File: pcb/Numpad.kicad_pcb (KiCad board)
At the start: 2 copper layers, 57 parts, among them P1 USB-MICRO-B, SW1 F1, SW10 8, SW11 9, SW12 PLUS, SW13 4, SW14 5, SW15 6, SW16 ENTER, SW17 1, SW18 2, SW19 3, SW2 F2, SW20 0, SW21 PERIOD, SW22 SW_PUSH, SW3 F3, SW4 F4, SW5 NUMLOCK, SW6 SLASH, SW7 STAR, SW8 MINUS, SW9 7, U1 ATmega32U4-AU, X1 16MHz

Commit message: Lay out components mostly
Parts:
- C1, C2, C3, C4, C5, C6, D1, D10, D11, D12, D13, D14, D15, D16, D17, D18, D19, D2, D20, D21, D3, D4, D5, D6, D7, D8, D9, P1, R1, R2, R3, R4, SW22, U1, X1: moved to B.Cu
- moved SW22 161.9 mm to (103.5, 132.7), turned to 270 degrees
- moved U1 135.2 mm to (132.1, 134.0)
- moved D17 129.5 mm to (74.9, 149.9), turned to 180 degrees
- moved D13 128.1 mm to (74.9, 130.8), turned to 180 degrees
- moved X1 127.6 mm to (132.1, 102.9), turned to 180 degrees
- moved D9 126.9 mm to (74.9, 111.8), turned to 180 degrees
- moved D5 125.3 mm to (74.9, 92.7), turned to 180 degrees
- moved D1 123.8 mm to (74.9, 73.7), turned to 180 degrees
- moved D20 123.8 mm to (84.5, 168.9), turned to 180 degrees
- moved C1 116.0 mm to (118.7, 127.6), turned to 270 degrees
- moved D18 110.4 mm to (94.0, 149.9), turned to 180 degrees
- moved R4 109.6 mm to (103.5, 139.7)
- moved D14 109.0 mm to (94.0, 130.8), turned to 180 degrees
- moved D10 107.6 mm to (94.0, 111.8), turned to 180 degrees
- moved P1 107.4 mm to (103.5, 59.1), turned to 0 degrees
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
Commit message: Add SMD micro USB B, move MCU
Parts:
- P1: footprint Connect:USB_Micro-B -> 10118192-0001LF:10118192-0001LF
- moved SW22 29.9 mm to (98.9, 162.3)
- moved R4 29.6 mm to (98.9, 168.9)
- moved R1 5.08 mm to (85.7, 66.7)
- moved R2 5.08 mm to (83.2, 66.7)
- moved P1 2.41 mm to (103.5, 56.6)
- moved U1 1.15 mm to (132.0, 132.8), turned to 225 degrees

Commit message: Add OSH Park design rules
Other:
- net class Default: clearance 0.2 -> 0.1524; trace_width 0.25 -> 0.1524; via_dia 0.6 -> 0.6858; via_drill 0.4 -> 0.3302
- rule trace_clearance: 0.2 -> 0.1524
- rule trace_min: 0.2 -> 0.1524
- rule via_min_drill: 0.3 -> 0.3302
- rule via_min_size: 0.4 -> 0.6858
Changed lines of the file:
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@@
   )
   (setup
-    (last_trace_width 0.25)
-    (trace_clearance 0.2)
+    (last_trace_width 0.1524)
+    (trace_clearance 0.1524)
     (zone_clearance 0.508)
     (zone_45_only no)
-    (trace_min 0.2)
+    (trace_min 0.1524)
     (segment_width 0.2)
     (edge_width 0.1)
-    (via_size 0.6)
-    (via_drill 0.4)
-    (via_min_size 0.4)
-    (via_min_drill 0.3)
-    (uvia_size 0.3)
-    (uvia_drill 0.1)
+    (via_size 0.6858)
+    (via_drill 0.3302)
+    (via_min_size 0.6858)
+    (via_min_drill 0.3302)
+    (uvia_size 0.762)
+    (uvia_drill 0.508)
     (uvias_allowed no)
-    (uvia_min_size 0.2)
-    (uvia_min_drill 0.1)
+    (uvia_min_size 0)
+    (uvia_min_drill 0)
     (pcb_text_width 0.3)
     (pcb_text_size 1.5 1.5)
@@
   (net 61 "Net-(U1-Pad42)")
   (net_class Default "This is the default net class."
-    (clearance 0.2)
-    (trace_width 0.25)
-    (via_dia 0.6)
-    (via_drill 0.4)
-    (uvia_dia 0.3)
-    (uvia_drill 0.1)
+    (clearance 0.1524)
+    (trace_width 0.1524)
+    (via_dia 0.6858)
+    (via_drill 0.3302)
+    (uvia_dia 0.762)
+    (uvia_drill 0.508)
     (add_net +5V)
     (add_net /COL0)

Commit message: Routing
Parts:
- added P2: HOLE, Connect:1pin, F.Cu at (84.2, 75.7)
- added P3: HOLE, Connect:1pin, F.Cu at (122.3, 75.7)
- added P4: HOLE, Connect:1pin, F.Cu at (84.5, 145.8)
- added P5: HOLE, Connect:1pin, F.Cu at (121.8, 152.4)
- moved D3 19.2 mm to (112.9, 73.7)
- moved D4 19.2 mm to (132.2, 73.7)
- moved R1 19.1 mm to (104.8, 65.7), turned to 90 degrees
- moved R2 19.1 mm to (102.2, 65.7), turned to 90 degrees
- moved SW3 19.1 mm to (113.0, 66.0)
- moved SW4 19.1 mm to (132.1, 66.0)
- moved R4 13.5 mm to (98.7, 155.4), turned to 180 degrees
- moved C5 6.35 mm to (103.5, 74.3)
- moved C4 6.35 mm to (103.5, 71.8)
- moved C6 6.35 mm to (103.5, 76.8)
- moved D13 4.21 mm to (71.2, 132.8), turned to 90 degrees
- moved D5 4.21 mm to (71.2, 94.7), turned to 90 degrees
- moved D1 4.09 mm to (71.2, 75.4), turned to 90 degrees
- moved D17 4.09 mm to (71.2, 151.6), turned to 90 degrees
- moved D9 4.09 mm to (71.2, 113.5), turned to 90 degrees
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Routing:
- net GND: track 0.00 -> 240.9 mm, vias 0 -> 1
- net /COL0: track 0.00 -> 152.9 mm, vias 0 -> 2
- net /ROW0: track 0.00 -> 143.0 mm, vias 0 -> 1
- net +5V: track 0.00 -> 111.7 mm, vias 0 -> 4
- net Net-(R1-Pad1): track 0.00 -> 106.9 mm, vias 0 -> 2
- net Net-(R2-Pad1): track 0.00 -> 106.9 mm, vias 0 -> 2
- net /COL3: track 0.00 -> 78.8 mm
- net /ROW1: track 0.00 -> 65.1 mm, vias 0 -> 1
- net /ROW3: track 0.00 -> 58.1 mm, vias 0 -> 1
- net /COL4: track 0.00 -> 52.9 mm, vias 0 -> 2
- net /ISP_RESET: track 0.00 -> 50.7 mm, vias 0 -> 2
- net /XTAL1: track 0.00 -> 45.1 mm, vias 0 -> 2
- net /COL1: track 0.00 -> 44.9 mm, vias 0 -> 2
- net /XTAL2: track 0.00 -> 41.0 mm, vias 0 -> 2
- net VCC: track 0.00 -> 38.3 mm, vias 0 -> 2
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
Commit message: Accidentally did most of the routing
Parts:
- moved D12 42.8 mm to (124.3, 117.1), turned to 90 degrees
- moved D16 41.7 mm to (128.4, 159.5), turned to 0 degrees
- moved SW12 38.1 mm to (132.1, 113.7)
- moved SW16 38.1 mm to (132.1, 151.8)
- moved C1 17.4 mm to (135.1, 121.7), turned to 180 degrees
- moved D8 4.10 mm to (128.5, 94.7), turned to 90 degrees
- moved D14 4.10 mm to (90.4, 132.8), turned to 90 degrees
- moved D6 4.10 mm to (90.4, 94.7), turned to 90 degrees
- moved D4 4.09 mm to (128.5, 75.4), turned to 90 degrees
- moved D2 3.98 mm to (90.4, 75.4), turned to 90 degrees
- moved D10 3.98 mm to (90.4, 113.5), turned to 90 degrees
- moved D18 3.98 mm to (90.4, 151.6), turned to 90 degrees
- moved D7 3.88 mm to (109.7, 94.7), turned to 90 degrees
- moved D11 3.75 mm to (109.7, 113.5), turned to 90 degrees
- moved D3 3.64 mm to (109.7, 75.4), turned to 90 degrees
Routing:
- net GND: track 240.9 -> 406.1 mm, vias 1 -> 7
- net /COL2: track 24.0 -> 129.4 mm, vias 2 -> 4
- net /COL1: track 44.9 -> 150.0 mm, vias 2 -> 4
- net /ROW4: track 19.4 -> 109.0 mm, vias 2 -> 1
- net /ROW2: track 16.1 -> 97.9 mm, vias 0 -> 1
- net /NUMLOCK_LED: track 0.00 -> 79.0 mm, vias 0 -> 6
- net /COL3: track 78.8 -> 155.5 mm, vias 0 -> 4
- net /ROW1: track 65.1 -> 122.2 mm
- net VCC: track 38.3 -> 86.8 mm, vias 2 -> 7
- net /ROW3: track 58.1 -> 104.9 mm, vias 1 -> 5
- net Net-(C1-Pad1): track 0.00 -> 16.3 mm, vias 0 -> 2
- net Net-(D19-Pad2): track 0.00 -> 11.1 mm
- net /COL0: track 152.9 -> 160.8 mm, vias 2 -> 6
- net +5V: track 111.7 -> 118.3 mm
- net Net-(D22-Pad2): track 0.00 -> 5.10 mm

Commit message: Finish routing
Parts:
- moved R2 2.01 mm to (102.9, 63.8)
- moved C1 2.01 mm to (135.8, 119.8)
- moved D16 2.01 mm to (129.0, 157.6)
- moved R1 2.01 mm to (105.4, 63.8)
- moved C3 2.01 mm to (127.6, 101.0)
- moved C4 2.01 mm to (104.1, 69.8)
- moved C5 2.01 mm to (104.1, 72.4)
- moved D1 2.01 mm to (71.9, 73.5)
- moved D11 2.01 mm to (110.4, 111.6)
- moved D12 2.01 mm to (125.0, 115.2)
- moved D13 2.01 mm to (71.9, 130.9)
- moved D15 2.01 mm to (113.7, 128.9)
- moved D17 2.01 mm to (71.9, 149.7)
- moved D19 2.01 mm to (113.7, 148.0)
- moved D20 2.01 mm to (85.1, 167.0)
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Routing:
- net Net-(D15-Pad2): track 0.00 -> 11.1 mm
- net Net-(D21-Pad2): track 0.00 -> 11.1 mm
- net Net-(D20-Pad2): track 0.00 -> 11.1 mm
- net Net-(D7-Pad2): track 0.00 -> 11.0 mm
- net Net-(D6-Pad2): track 0.00 -> 11.0 mm
- net Net-(D4-Pad2): track 0.00 -> 10.8 mm
- net Net-(D3-Pad2): track 0.00 -> 10.8 mm
- net Net-(D2-Pad2): track 0.00 -> 10.8 mm
- net Net-(D8-Pad2): track 0.00 -> 10.7 mm
- net Net-(D14-Pad2): track 0.00 -> 10.7 mm
- net Net-(D11-Pad2): track 0.00 -> 10.5 mm
- net Net-(D18-Pad2): track 0.00 -> 10.4 mm
- net Net-(D10-Pad2): track 0.00 -> 10.4 mm
- net Net-(D12-Pad2): track 0.00 -> 6.04 mm
- net Net-(D16-Pad2): track 0.00 -> 4.14 mm
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
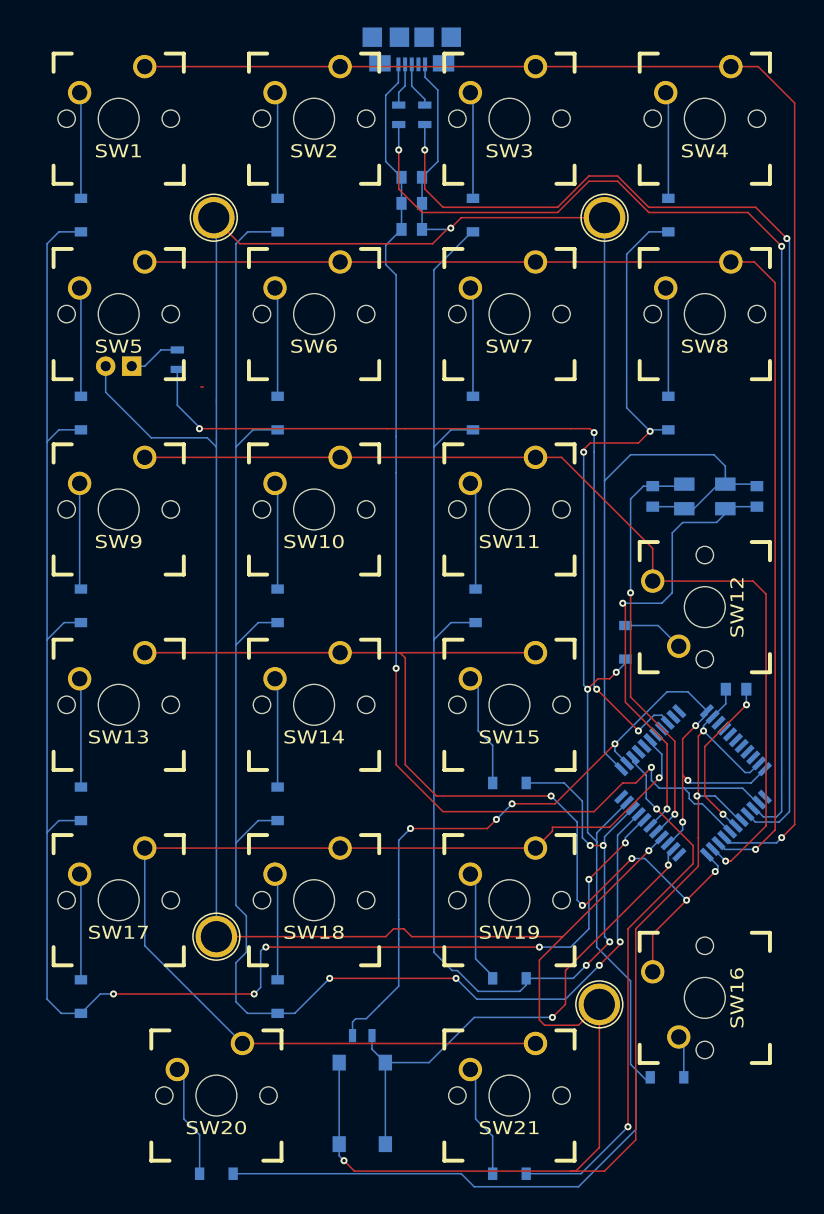
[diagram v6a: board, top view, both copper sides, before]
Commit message: Add edge cuts
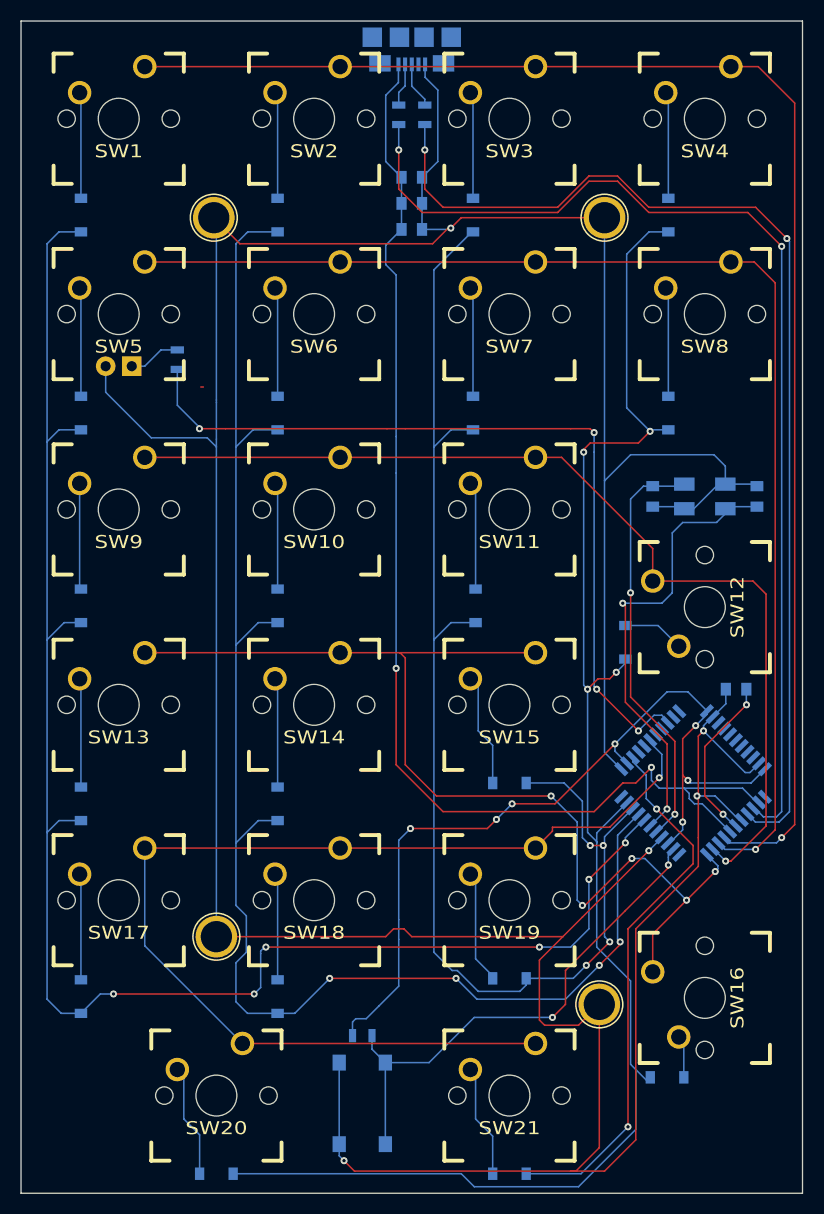
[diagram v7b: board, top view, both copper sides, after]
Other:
- board outline added: 76.2 x 114.3 mm
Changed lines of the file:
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@@
     (links 106)
     (no_connects 0)
-    (area 65.303399 55.114199 141.706601 172.0374)
+    (area 65.989999 54.559999 142.290001 168.960001)
     (thickness 1.6)
-    (drawings 0)
+    (drawings 4)
     (tracks 561)
     (zones 0)
@@
       (net 2 GND))
   )
+  (gr_line (start 66.04 168.91) (end 66.04 54.61) (angle 90) (layer Edge.Cuts) (width 0.1))
+  (gr_line (start 142.24 168.91) (end 66.04 168.91) (angle 90) (layer Edge.Cuts) (width 0.1))
+  (gr_line (start 142.24 54.61) (end 142.24 168.91) (angle 90) (layer Edge.Cuts) (width 0.1))
+  (gr_line (start 66.04 54.61) (end 142.24 54.61) (angle 90) (layer Edge.Cuts) (width 0.1))
   (segment (start 83.566 90.297) (end 83.82 90.297) (width 0.1524) (layer F.Cu) (net 0))
   (segment (start 136.763 119.761) (end 136.763 121.269) (width 0.1524) (layer B.Cu) (net 1))
